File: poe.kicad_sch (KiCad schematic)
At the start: 59 parts, among them IC1 TPS2378DDA, J1 B2B-XH-A_LF__SN_, J6 SS-74800-144, U3 TPS2373-3RGW, U4 URB4805YMD-30WR3

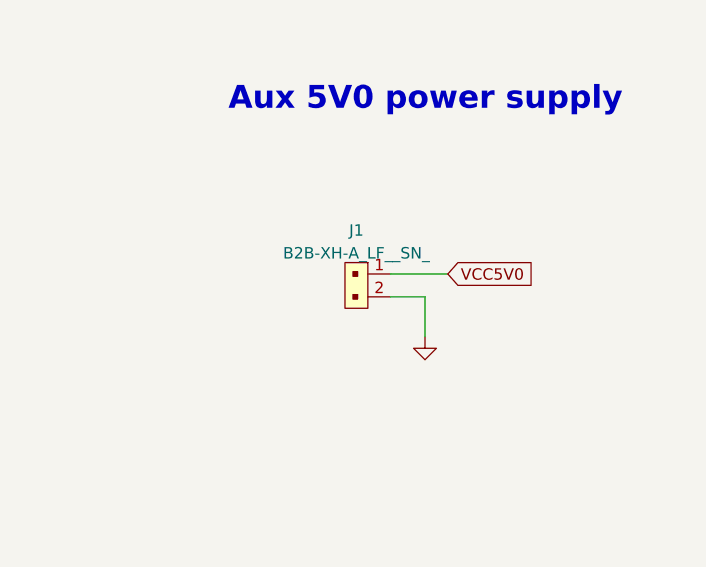
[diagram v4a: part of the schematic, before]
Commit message: Update J1 symbol and footprint
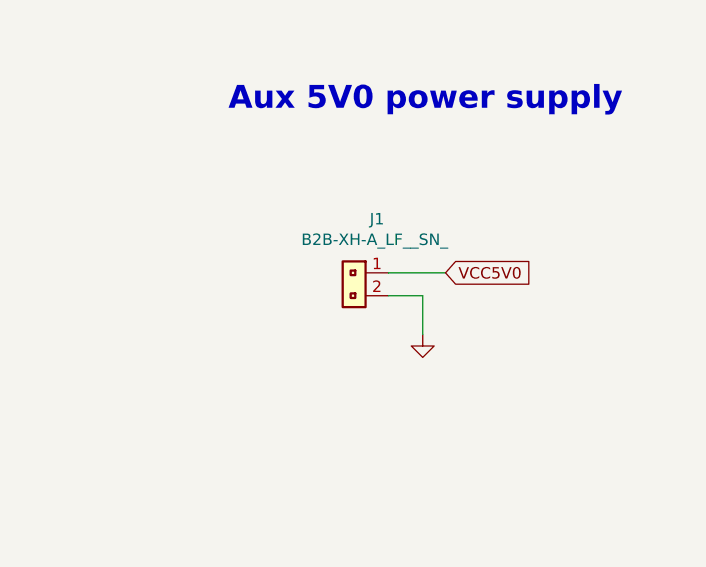
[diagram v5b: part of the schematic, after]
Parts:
- J1: footprint scalenode-cm4-baseboard-footprints:PinHeader_1x2_P2.5mm_Drill1.1mm -> antmicro-footprints:PinHeader_1x2_P2.5mm_Drill1.1mm; symbol scalenode-cm4-baseboard:B2B-XH-A_LF__SN_ -> antmicroRectangularConnectorsHeadersMalePins:B2B-XH-A_LF__SN_; Author (none) -> Antmicro; License (none) -> Apache-2.0; Manufacturer JST Sales America Inc. -> JST
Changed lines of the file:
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@@
     (stroke (width 0) (type default) (color 0 0 0 0))
   )
-  (wire (pts (xy 337.82 74.549) (xy 341.63 74.549))
+  (wire (pts (xy 337.566 74.422) (xy 341.376 74.422))
     (stroke (width 0) (type default) (color 0 0 0 0))
   )
@@
     (stroke (width 0) (type default) (color 0 0 0 0))
   )
-  (wire (pts (xy 341.63 74.549) (xy 341.63 78.994))
+  (wire (pts (xy 341.376 74.422) (xy 341.376 78.74))
     (stroke (width 0) (type default) (color 0 0 0 0))
   )
@@
     (stroke (width 0) (type default) (color 0 0 0 0))
   )
-  (wire (pts (xy 344.17 72.009) (xy 337.82 72.009))
+  (wire (pts (xy 343.916 71.882) (xy 337.566 71.882))
     (stroke (width 0) (type default) (color 0 0 0 0))
   )
@@
     )
   )
-  (global_label "VCC5V0" (shape input) (at 344.17 72.009 0) (fields_autoplaced)
+  (global_label "VCC5V0" (shape input) (at 343.916 71.882 0) (fields_autoplaced)
     (effects (font (size 1.27 1.27)) (justify left))
-    (property "Intersheet References" "${INTERSHEET_REFS}" (id 0) (at -40.005 42.799 0)
+    (property "Intersheet References" "${INTERSHEET_REFS}" (id 0) (at -40.259 42.672 0)
       (effects (font (size 1.27 1.27)) hide)
     )
@@
     (pin "K")
   )
-  (symbol (lib_id "scalenode-cm4-baseboard:B2B-XH-A_LF__SN_") (at 335.28 72.009 270) (unit 1)
-    (in_bom yes) (on_board yes) (fields_autoplaced)
-    (property "Reference" "J1" (id 0) (at 334.01 67.1662 90))
-    (property "Value" "B2B-XH-A_LF__SN_" (id 1) (at 334.01 69.7031 90))
-    (property "Footprint" "scalenode-cm4-baseboard-footprints:PinHeader_1x2_P2.5mm_Drill1.1mm" (id 2) (at 340.36 77.089 0)
-      (effects (font (size 1.524 1.524)) (justify left) hide)
+  (symbol (lib_id "antmicroRectangularConnectorsHeadersMalePins:B2B-XH-A_LF__SN_") (at 337.566 71.882 270) (unit 1)
+    (in_bom yes) (on_board yes)
+    (property "Reference" "J1" (id 0) (at 336.296 65.913 90))
+    (property "Value" "B2B-XH-A_LF__SN_" (id 1) (at 336.042 68.199 90))
+    (property "Footprint" "antmicro-footprints:PinHeader_1x2_P2.5mm_Drill1.1mm" (id 2) (at 333.756 79.502 0)
+      (effects (font (size 1.27 1.27) (thickness 0.15)) (justify left bottom) hide)
     )
-    (property "Datasheet" "http://www.jst-mfg.com/product/pdf/eng/eXH.pdf" (id 3) (at 342.9 77.089 0)
-      (effects (font (size 1.524 1.524)) (justify left) hide)
+    (property "Datasheet" "http://www.jst-mfg.com/product/pdf/eng/eXH.pdf" (id 3) (at 331.216 79.502 0)
+      (effects (font (size 1.27 1.27) (thickness 0.15)) (justify left bottom) hide)
     )
-    (property "MPN" "B2B-XH-A(LF)(SN)" (id 4) (at 347.98 77.089 0)
-      (effects (font (size 1.524 1.524)) (justify left) hide)
+    (property "MPN" "B2B-XH-A(LF)(SN)" (id 4) (at 328.676 79.502 0)
+      (effects (font (size 1.27 1.27) (thickness 0.15)) (justify left bottom) hide)
     )
-    (property "Manufacturer" "JST Sales America Inc." (id 5) (at 363.22 77.089 0)
-      (effects (font (size 1.524 1.524)) (justify left) hide)
+    (property "Manufacturer" "JST" (id 5) (at 326.136 79.502 0)
+      (effects (font (size 1.27 1.27) (thickness 0.15)) (justify left bottom) hide)
+    )
+    (property "Author" "Antmicro" (id 6) (at 323.596 79.502 0)
+      (effects (font (size 1.27 1.27) (thickness 0.15)) (justify left bottom) hide)
+    )
+    (property "License" "Apache-2.0" (id 7) (at 321.056 79.502 0)
+      (effects (font (size 1.27 1.27) (thickness 0.15)) (justify left bottom) hide)
     )
     (pin "1")
@@
     (pin "2")
   )
-  (symbol (lib_id "scalenode-cm4-baseboard:GND") (at 341.63 78.994 0) (unit 1)
+  (symbol (lib_id "scalenode-cm4-baseboard:GND") (at 341.376 78.74 0) (unit 1)
     (in_bom yes) (on_board yes)
-    (property "Reference" "#PWR022" (id 0) (at 341.63 85.344 0)
+    (property "Reference" "#PWR022" (id 0) (at 341.376 85.09 0)
       (effects (font (size 1.27 1.27)) hide)
     )
-    (property "Value" "~" (id 1) (at 341.757 83.3882 0))
-    (property "Footprint" "" (id 2) (at 341.63 78.994 0)
+    (property "Value" "~" (id 1) (at 341.503 83.1342 0))
+    (property "Footprint" "" (id 2) (at 341.376 78.74 0)
       (effects (font (size 1.27 1.27)) hide)
     )
-    (property "Datasheet" "" (id 3) (at 341.63 78.994 0)
+    (property "Datasheet" "" (id 3) (at 341.376 78.74 0)
       (effects (font (size 1.27 1.27)) hide)
     )

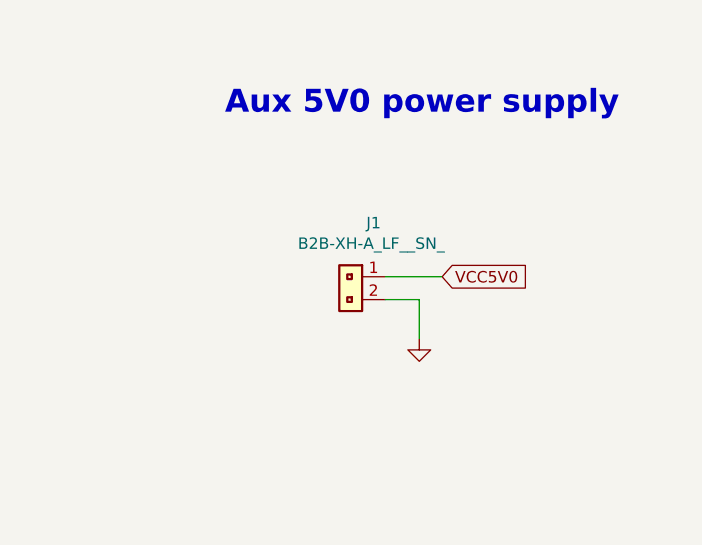
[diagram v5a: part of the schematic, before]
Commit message: Update J1 symbol
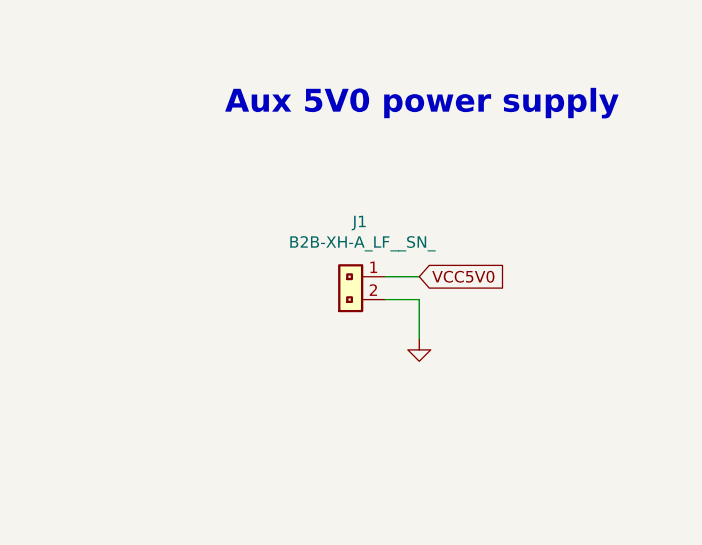
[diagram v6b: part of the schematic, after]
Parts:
- J1: symbol antmicroRectangularConnectorsHeadersMalePins:B2B-XH-A_LF__SN_ -> antmicroRectangularConnectorsHeadersMalePins:PinHeader_1x2_P2.5mm_Drill1.1mm
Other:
- moved on the sheet: J1
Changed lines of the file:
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@@
     (stroke (width 0) (type default) (color 0 0 0 0))
   )
-  (wire (pts (xy 343.916 71.882) (xy 337.566 71.882))
+  (wire (pts (xy 341.376 71.882) (xy 337.566 71.882))
     (stroke (width 0) (type default) (color 0 0 0 0))
   )
@@
     )
   )
-  (global_label "VCC5V0" (shape input) (at 343.916 71.882 0) (fields_autoplaced)
+  (global_label "VCC5V0" (shape input) (at 341.376 71.882 0) (fields_autoplaced)
     (effects (font (size 1.27 1.27)) (justify left))
-    (property "Intersheet References" "${INTERSHEET_REFS}" (id 0) (at -40.259 42.672 0)
+    (property "Intersheet References" "${INTERSHEET_REFS}" (id 0) (at -42.799 42.672 0)
       (effects (font (size 1.27 1.27)) hide)
     )
@@
     (pin "K")
   )
-  (symbol (lib_id "antmicroRectangularConnectorsHeadersMalePins:B2B-XH-A_LF__SN_") (at 337.566 71.882 270) (unit 1)
+  (symbol (lib_id "antmicroRectangularConnectorsHeadersMalePins:PinHeader_1x2_P2.5mm_Drill1.1mm") (at 337.566 71.882 0) (mirror y) (unit 1)
     (in_bom yes) (on_board yes)
-    (property "Reference" "J1" (id 0) (at 336.296 65.913 90))
-    (property "Value" "B2B-XH-A_LF__SN_" (id 1) (at 336.042 68.199 90))
-    (property "Footprint" "antmicro-footprints:PinHeader_1x2_P2.5mm_Drill1.1mm" (id 2) (at 333.756 79.502 0)
+    (property "Reference" "J1" (id 0) (at 334.772 65.786 0))
+    (property "Value" "B2B-XH-A_LF__SN_" (id 1) (at 335.026 68.072 0))
+    (property "Footprint" "antmicro-footprints:PinHeader_1x2_P2.5mm_Drill1.1mm" (id 2) (at 329.946 75.692 0)
       (effects (font (size 1.27 1.27) (thickness 0.15)) (justify left bottom) hide)
     )
-    (property "Datasheet" "http://www.jst-mfg.com/product/pdf/eng/eXH.pdf" (id 3) (at 331.216 79.502 0)
+    (property "Datasheet" "http://www.jst-mfg.com/product/pdf/eng/eXH.pdf" (id 3) (at 329.946 78.232 0)
       (effects (font (size 1.27 1.27) (thickness 0.15)) (justify left bottom) hide)
     )
-    (property "MPN" "B2B-XH-A(LF)(SN)" (id 4) (at 328.676 79.502 0)
+    (property "MPN" "B2B-XH-A(LF)(SN)" (id 4) (at 329.946 80.772 0)
       (effects (font (size 1.27 1.27) (thickness 0.15)) (justify left bottom) hide)
     )
-    (property "Manufacturer" "JST" (id 5) (at 326.136 79.502 0)
+    (property "Manufacturer" "JST" (id 5) (at 329.946 83.312 0)
       (effects (font (size 1.27 1.27) (thickness 0.15)) (justify left bottom) hide)
     )
-    (property "Author" "Antmicro" (id 6) (at 323.596 79.502 0)
+    (property "Author" "Antmicro" (id 6) (at 329.946 85.852 0)
       (effects (font (size 1.27 1.27) (thickness 0.15)) (justify left bottom) hide)
     )
-    (property "License" "Apache-2.0" (id 7) (at 321.056 79.502 0)
+    (property "License" "Apache-2.0" (id 7) (at 329.946 88.392 0)
       (effects (font (size 1.27 1.27) (thickness 0.15)) (justify left bottom) hide)
     )
@@
       (effects (font (size 1.27 1.27) (thickness 0.15)) (justify left bottom) hide)
     )
-    (property "Author" "Antmicro" (id 7) (at 314.706 210.566 0)
+    (property "Author" "Antmicro" (id 8) (at 314.706 210.566 0)
       (effects (font (size 1.27 1.27) (thickness 0.15)) (justify left bottom) hide)
     )

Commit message: Update FB1 FB2 symbol and footprint
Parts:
- FB1, FB2: footprint antmicro-footprints:0805-res -> antmicro-footprints:FB_0805_2012Metric; symbol antmicroFuses:BLM21PG221SN1D -> antmicroFuses:F_1.25A_0805
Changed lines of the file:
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@@
     (pin "2")
   )
-  (symbol (lib_id "antmicroFuses:BLM21PG221SN1D") (at 85.852 179.832 0) (unit 1)
+  (symbol (lib_id "antmicroFuses:F_1.25A_0805") (at 85.852 179.832 0) (unit 1)
     (in_bom yes) (on_board yes)
     (property "Reference" "FB1" (id 0) (at 85.217 176.022 0)
@@
       (effects (font (size 1.524 1.524)))
     )
-    (property "Footprint" "antmicro-footprints:0805-res" (id 2) (at 111.252 187.452 0)
+    (property "Footprint" "antmicro-footprints:FB_0805_2012Metric" (id 2) (at 111.252 187.452 0)
       (effects (font (size 1.27 1.27) (thickness 0.15)) (justify left bottom) hide)
     )
-    (property "Datasheet" "" (id 3) (at 111.252 189.992 0)
+    (property "Datasheet" "https://www.mouser.pl/datasheet/2/281/1/mure_s_a0010614409_1-2279304.pdf" (id 3) (at 111.252 189.992 0)
       (effects (font (size 1.27 1.27) (thickness 0.15)) (justify left bottom) hide)
     )
@@
     (pin "2")
   )
-  (symbol (lib_id "antmicroFuses:BLM21PG221SN1D") (at 86.36 149.86 0) (unit 1)
+  (symbol (lib_id "antmicroFuses:F_1.25A_0805") (at 86.36 149.86 0) (unit 1)
     (in_bom yes) (on_board yes)
     (property "Reference" "FB2" (id 0) (at 85.725 145.415 0)
@@
       (effects (font (size 1.524 1.524)))
     )
-    (property "Footprint" "antmicro-footprints:0805-res" (id 2) (at 111.76 157.48 0)
+    (property "Footprint" "antmicro-footprints:FB_0805_2012Metric" (id 2) (at 111.76 157.48 0)
       (effects (font (size 1.27 1.27) (thickness 0.15)) (justify left bottom) hide)
     )
-    (property "Datasheet" "" (id 3) (at 111.76 160.02 0)
+    (property "Datasheet" "https://www.mouser.pl/datasheet/2/281/1/mure_s_a0010614409_1-2279304.pdf" (id 3) (at 111.76 160.02 0)
       (effects (font (size 1.27 1.27) (thickness 0.15)) (justify left bottom) hide)
     )

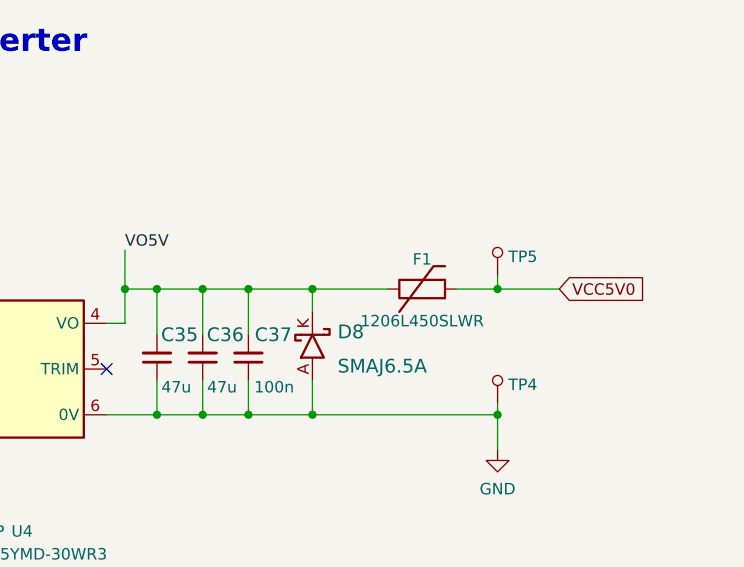
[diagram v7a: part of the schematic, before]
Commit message: Update F1 symbol and schematic
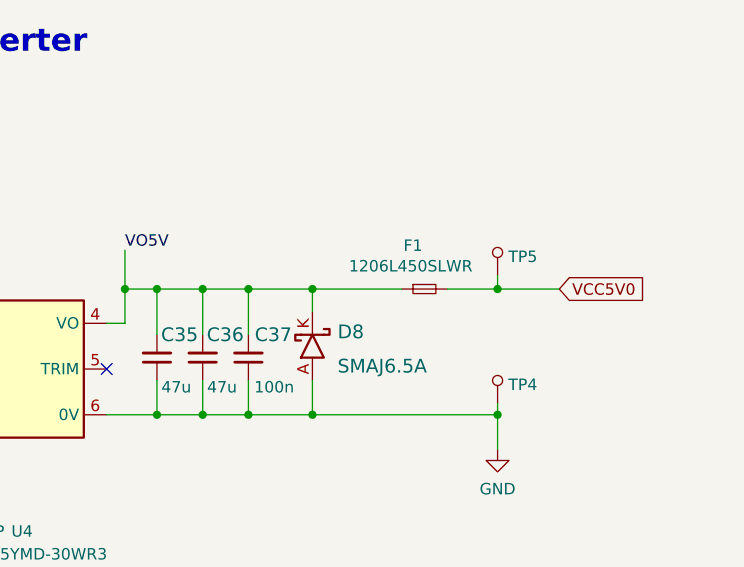
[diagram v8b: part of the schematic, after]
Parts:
- F1: footprint scalenode-cm4-baseboard-footprints:1206-res -> antmicro-footprints:F_1206_3216Metric; symbol scalenode-cm4-baseboard:1206L450SLWR -> antmicroFuses:F_4.5A_1206; Author (none) -> Antmicro; License (none) -> Apache-2.0; Manufacturer LITTELFUSE -> Littelfuse
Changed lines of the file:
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@@
     (stroke (width 0) (type default) (color 0 0 0 0))
   )
-  (wire (pts (xy 324.866 186.436) (xy 333.248 186.436))
+  (wire (pts (xy 324.866 186.436) (xy 334.772 186.436))
     (stroke (width 0) (type default) (color 0 0 0 0))
   )
@@
     (stroke (width 0) (type default) (color 0 0 0 0))
   )
-  (wire (pts (xy 340.868 186.436) (xy 345.44 186.436))
+  (wire (pts (xy 339.852 186.436) (xy 345.44 186.436))
     (stroke (width 0) (type default) (color 0 0 0 0))
   )
@@
     (pin "9")
   )
-  (symbol (lib_id "scalenode-cm4-baseboard:1206L450SLWR") (at 337.058 186.436 0) (unit 1)
+  (symbol (lib_id "antmicroFuses:F_4.5A_1206") (at 334.772 186.436 0) (unit 1)
     (in_bom yes) (on_board yes)
-    (property "Reference" "F1" (id 0) (at 337.058 183.134 0))
-    (property "Value" "1206L450SLWR" (id 1) (at 337.058 189.992 0))
-    (property "Footprint" "scalenode-cm4-baseboard-footprints:1206-res" (id 2) (at 338.328 192.151 0)
-      (effects (font (size 1.27 1.27)) hide)
+    (property "Reference" "F1" (id 0) (at 336.042 181.61 0))
+    (property "Value" "1206L450SLWR" (id 1) (at 335.788 183.896 0))
+    (property "Footprint" "antmicro-footprints:F_1206_3216Metric" (id 2) (at 348.742 191.516 0)
+      (effects (font (size 1.27 1.27) (thickness 0.15)) (justify left bottom) hide)
     )
-    (property "Datasheet" "http://www.farnell.com/datasheets/2282556.pdf" (id 3) (at 337.058 190.246 0)
-      (effects (font (size 1.27 1.27)) hide)
+    (property "Datasheet" "http://www.farnell.com/datasheets/2282556.pdf" (id 3) (at 348.742 194.056 0)
+      (effects (font (size 1.27 1.27) (thickness 0.15)) (justify left bottom) hide)
     )
-    (property "MPN" "1206L450SLWR" (id 4) (at 337.693 194.056 0)
-      (effects (font (size 1.27 1.27)) hide)
+    (property "MPN" "1206L450SLWR" (id 4) (at 348.742 196.596 0)
+      (effects (font (size 1.27 1.27) (thickness 0.15)) (justify left bottom) hide)
     )
-    (property "Manufacturer" "LITTELFUSE" (id 5) (at 338.328 195.961 0)
-      (effects (font (size 1.27 1.27)) hide)
+    (property "Manufacturer" "Littelfuse" (id 5) (at 348.742 199.136 0)
+      (effects (font (size 1.27 1.27) (thickness 0.15)) (justify left bottom) hide)
+    )
+    (property "Author" "Antmicro" (id 6) (at 348.742 201.676 0)
+      (effects (font (size 1.27 1.27) (thickness 0.15)) (justify left bottom) hide)
+    )
+    (property "License" "Apache-2.0" (id 7) (at 348.742 204.216 0)
+      (effects (font (size 1.27 1.27) (thickness 0.15)) (justify left bottom) hide)
     )
     (pin "1")
